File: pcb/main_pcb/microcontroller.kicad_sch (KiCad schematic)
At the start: 20 parts, among them J1 Conn_01x05, J10 Conn_01x06_Male, J2 Conn_01x05, J3 Conn_01x05, J4 Conn_01x05, J5 Conn_01x05, J6 Conn_01x05, J8 Conn_01x06_Male, U3 DRV8833

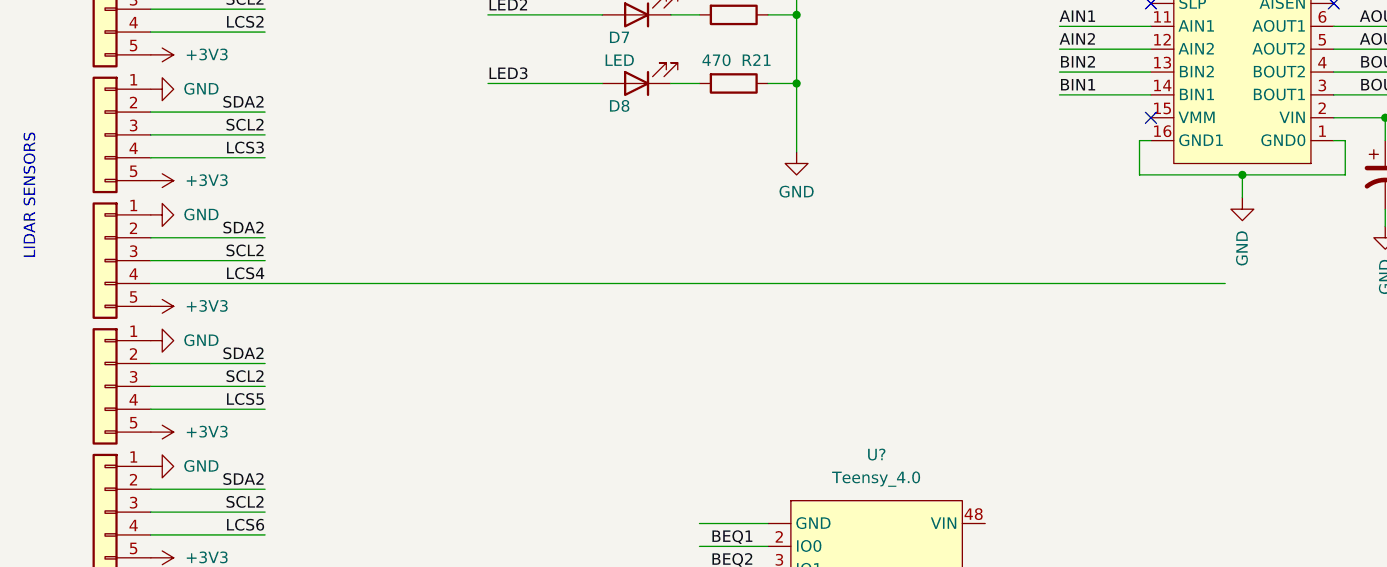
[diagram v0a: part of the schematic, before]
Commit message: Deleted old 3v3 power supply
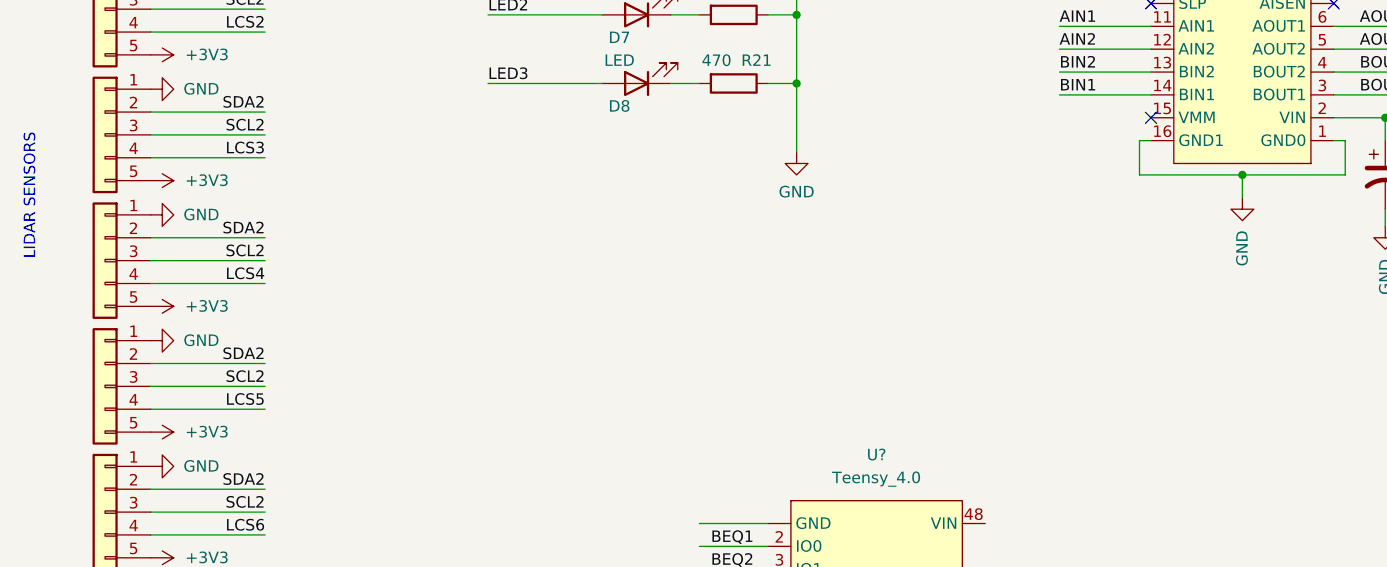
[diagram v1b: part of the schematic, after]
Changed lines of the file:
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@@
-    (stroke (width 0) (type default) (color 0 0 0 0))
-  )
-  (wire (pts (xy 35.56 81.28) (xy 154.94 81.28))
     (stroke (width 0) (type default) (color 0 0 0 0))
   )
@@
     (stroke (width 0) (type default) (color 0 0 0 0))
   )
+  (wire (pts (xy 35.56 81.28) (xy 48.26 81.28))
+    (stroke (width 0) (type default) (color 0 0 0 0))
+  )

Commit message: changes to pcb
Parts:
- gave numbers to parts that had none: 2
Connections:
- net LCS2: now reaches U2. (VBat)
- net LCS2: now also J2.4 (Pin_4)
- net LCS1: now reaches U2.20 (IO18)
- net LCS1: now also J1.4 (Pin_4)
- net LCS5: now reaches U2.22 (IO16)
- net LCS5: now also J5.4 (Pin_4)
- net LCS6: now reaches U2.23 (IO15)
- net LCS6: now also J6.4 (Pin_4)
- net LCS7: now reaches U2.24 (IO14)
- net LCS7: now also J7.4 (Pin_4)
- net LCS4: now reaches U2.8 (IO6)
- net LCS4: now also J4.4 (Pin_4)
- removed net ICSFRN: J1.4 (Pin_4), J2.4 (Pin_4), J3.4 (Pin_4), J4.4 (Pin_4), J5.4 (Pin_4), J6.4 (Pin_4), J7.4 (Pin_4), U2. (VBat), U2.16 (IO22)
- new net LCS3: J3.4 (Pin_4), U2.16 (IO22)
- no-connect marks 14 -> 9
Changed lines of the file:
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@@
   (junction (at 172.72 62.865) (diameter 0) (color 0 0 0 0)
   )
-  (junction (at 149.86 128.27) (diameter 0) (color 0 0 0 0)
-  )
-  (junction (at 149.86 130.81) (diameter 0) (color 0 0 0 0)
-  )
-  (junction (at 149.86 133.35) (diameter 0) (color 0 0 0 0)
-  )
   (junction (at 107.315 43.815) (diameter 0) (color 0 0 0 0)
   )
   (junction (at 156.845 69.215) (diameter 0) (color 0 0 0 0)
   )
-  (junction (at 149.86 135.89) (diameter 0) (color 0 0 0 0)
-  )
   (junction (at 107.315 51.435) (diameter 0) (color 0 0 0 0)
   )
-  (junction (at 149.86 125.73) (diameter 0) (color 0 0 0 0)
-  )
   (junction (at 107.315 59.055) (diameter 0) (color 0 0 0 0)
   )
-  (no_connect (at 128.27 135.89))
-  (no_connect (at 128.27 138.43))
-  (no_connect (at 104.14 125.73))
-  (no_connect (at 128.27 133.35))
   (no_connect (at 146.685 50.165))
-  (no_connect (at 128.27 128.27))
   (no_connect (at 167.005 47.625))
   (no_connect (at 146.685 62.865))
@@
     (stroke (width 0) (type default) (color 0 0 0 0))
   )
+  (wire (pts (xy 128.27 118.11) (xy 134.62 118.11))
+    (stroke (width 0) (type default) (color 0 0 0 0))
+  )
   (wire (pts (xy 85.725 51.435) (xy 73.025 51.435))
     (stroke (width 0) (type default) (color 0 0 0 0))
@@
     (stroke (width 0) (type default) (color 0 0 0 0))
   )
-  (wire (pts (xy 149.86 130.81) (xy 149.86 133.35))
-    (stroke (width 0) (type default) (color 0 0 0 0))
-  )
   (wire (pts (xy 35.56 78.74) (xy 48.26 78.74))
     (stroke (width 0) (type default) (color 0 0 0 0))
@@
     (stroke (width 0) (type default) (color 0 0 0 0))
   )
-  (wire (pts (xy 144.78 118.11) (xy 144.78 125.73))
-    (stroke (width 0) (type default) (color 0 0 0 0))
-  )
   (wire (pts (xy 96.52 133.35) (xy 104.14 133.35))
     (stroke (width 0) (type default) (color 0 0 0 0))
@@
     (stroke (width 0) (type default) (color 0 0 0 0))
   )
-  (wire (pts (xy 128.27 118.11) (xy 144.78 118.11))
+  (wire (pts (xy 128.27 138.43) (xy 135.89 138.43))
     (stroke (width 0) (type default) (color 0 0 0 0))
   )
@@
     (stroke (width 0) (type default) (color 0 0 0 0))
   )
-  (wire (pts (xy 144.78 125.73) (xy 149.86 125.73))
-    (stroke (width 0) (type default) (color 0 0 0 0))
-  )
   (wire (pts (xy 247.65 62.865) (xy 243.84 62.865))
     (stroke (width 0) (type default) (color 0 0 0 0))
@@
     (stroke (width 0) (type default) (color 0 0 0 0))
   )
-  (wire (pts (xy 149.86 125.73) (xy 154.94 125.73))
-    (stroke (width 0) (type default) (color 0 0 0 0))
-  )
   (wire (pts (xy 35.56 67.31) (xy 48.26 67.31))
     (stroke (width 0) (type default) (color 0 0 0 0))
@@
     (stroke (width 0) (type default) (color 0 0 0 0))
   )
+  (wire (pts (xy 128.27 135.89) (xy 135.89 135.89))
+    (stroke (width 0) (type default) (color 0 0 0 0))
+  )
   (wire (pts (xy 107.315 43.815) (xy 107.315 51.435))
     (stroke (width 0) (type default) (color 0 0 0 0))
@@
     (stroke (width 0) (type default) (color 0 0 0 0))
   )
-  (wire (pts (xy 149.86 125.73) (xy 149.86 128.27))
-    (stroke (width 0) (type default) (color 0 0 0 0))
-  )
   (wire (pts (xy 35.56 76.2) (xy 48.26 76.2))
     (stroke (width 0) (type default) (color 0 0 0 0))
@@
     (stroke (width 0) (type default) (color 0 0 0 0))
   )
+  (wire (pts (xy 128.27 128.27) (xy 135.89 128.27))
+    (stroke (width 0) (type default) (color 0 0 0 0))
+  )
   (wire (pts (xy 107.315 59.055) (xy 107.315 66.675))
     (stroke (width 0) (type default) (color 0 0 0 0))
   )
-  (wire (pts (xy 149.86 135.89) (xy 149.86 138.43))
-    (stroke (width 0) (type default) (color 0 0 0 0))
-  )
-  (wire (pts (xy 149.86 128.27) (xy 149.86 130.81))
-    (stroke (width 0) (type default) (color 0 0 0 0))
-  )
   (wire (pts (xy 146.685 55.245) (xy 136.525 55.245))
     (stroke (width 0) (type default) (color 0 0 0 0))
@@
     (stroke (width 0) (type default) (color 0 0 0 0))
   )
-  (wire (pts (xy 149.86 138.43) (xy 154.94 138.43))
-    (stroke (width 0) (type default) (color 0 0 0 0))
-  )
   (wire (pts (xy 35.56 121.92) (xy 48.26 121.92))
     (stroke (width 0) (type default) (color 0 0 0 0))
@@
     (stroke (width 0) (type default) (color 0 0 0 0))
   )
-  (wire (pts (xy 149.86 128.27) (xy 154.94 128.27))
-    (stroke (width 0) (type default) (color 0 0 0 0))
-  )
   (wire (pts (xy 202.565 45.085) (xy 202.565 55.245))
     (stroke (width 0) (type default) (color 0 0 0 0))
@@
     (stroke (width 0) (type default) (color 0 0 0 0))
   )
+  (wire (pts (xy 96.52 125.73) (xy 104.14 125.73))
+    (stroke (width 0) (type default) (color 0 0 0 0))
+  )
   (wire (pts (xy 104.14 59.055) (xy 107.315 59.055))
     (stroke (width 0) (type default) (color 0 0 0 0))
@@
     (stroke (width 0) (type default) (color 0 0 0 0))
   )
-  (wire (pts (xy 149.86 133.35) (xy 154.94 133.35))
-    (stroke (width 0) (type default) (color 0 0 0 0))
-  )
-  (wire (pts (xy 149.86 135.89) (xy 154.94 135.89))
-    (stroke (width 0) (type default) (color 0 0 0 0))
-  )
-  (wire (pts (xy 149.86 130.81) (xy 154.94 130.81))
-    (stroke (width 0) (type default) (color 0 0 0 0))
-  )
   (wire (pts (xy 35.56 109.22) (xy 48.26 109.22))
     (stroke (width 0) (type default) (color 0 0 0 0))
@@
     (stroke (width 0) (type default) (color 0 0 0 0))
   )
-  (wire (pts (xy 149.86 133.35) (xy 149.86 135.89))
-    (stroke (width 0) (type default) (color 0 0 0 0))
-  )
-  (wire (pts (xy 149.86 125.73) (xy 149.86 123.19))
-    (stroke (width 0) (type default) (color 0 0 0 0))
-  )
   (wire (pts (xy 93.345 43.815) (xy 96.52 43.815))
     (stroke (width 0) (type default) (color 0 0 0 0))
@@
     (stroke (width 0) (type default) (color 0 0 0 0))
   )
+  (wire (pts (xy 128.27 133.35) (xy 135.89 133.35))
+    (stroke (width 0) (type default) (color 0 0 0 0))
+  )
   (wire (pts (xy 35.56 64.77) (xy 48.26 64.77))
     (stroke (width 0) (type default) (color 0 0 0 0))
@@
   )
   (wire (pts (xy 191.135 60.325) (xy 203.835 60.325))
-    (stroke (width 0) (type default) (color 0 0 0 0))
-  )
-  (wire (pts (xy 149.86 123.19) (xy 154.94 123.19))
     (stroke (width 0) (type default) (color 0 0 0 0))
   )
@@
     (effects (font (size 1.27 1.27)) (justify right bottom))
   )
-  (label "LCS4" (at 149.86 130.81 0)
+  (label "LCS4" (at 96.52 125.73 0)
     (effects (font (size 1.27 1.27)) (justify left bottom))
   )
@@
     (effects (font (size 1.27 1.27)) (justify right bottom))
   )
-  (label "LCS7" (at 149.86 138.43 0)
+  (label "LCS7" (at 129.54 138.43 0)
     (effects (font (size 1.27 1.27)) (justify left bottom))
   )
@@
     (effects (font (size 1.27 1.27)) (justify left bottom))
   )
-  (label "ICSFRN" (at 128.27 115.57 0)
-    (effects (font (size 1.27 1.27)) (justify left bottom))
-  )
-  (label "LCS2" (at 149.86 125.73 0)
+  (label "LCS2" (at 129.54 115.57 0)
     (effects (font (size 1.27 1.27)) (justify left bottom))
   )
@@
     (effects (font (size 1.27 1.27)) (justify left bottom))
   )
-  (label "LCS3" (at 149.86 128.27 0)
-    (effects (font (size 1.27 1.27)) (justify left bottom))
-  )
   (label "LED2" (at 129.54 123.19 0)
     (effects (font (size 1.27 1.27)) (justify left bottom))
   )
-  (label "LCS1" (at 149.86 123.19 0)
+  (label "LCS1" (at 129.54 128.27 0)
     (effects (font (size 1.27 1.27)) (justify left bottom))
   )
@@
     (effects (font (size 1.27 1.27)) (justify left bottom))
   )
-  (label "ICSFRN" (at 128.27 118.11 0)
-    (effects (font (size 1.27 1.27)) (justify left bottom))
-  )
   (label "LED1" (at 97.79 123.19 0)
     (effects (font (size 1.27 1.27)) (justify left bottom))
   )
+  (label "LCS3" (at 129.54 118.11 0)
+    (effects (font (size 1.27 1.27)) (justify left bottom))
+  )
   (label "SCL2" (at 129.54 130.81 0)
     (effects (font (size 1.27 1.27)) (justify left bottom))
@@
     (effects (font (size 1.27 1.27)) (justify right bottom))
   )
+  (label "LCS6" (at 129.54 135.89 0)
+    (effects (font (size 1.27 1.27)) (justify left bottom))
+  )
   (label "SCL2" (at 48.26 92.71 180)
     (effects (font (size 1.27 1.27)) (justify right bottom))
@@
     (effects (font (size 1.27 1.27)) (justify left bottom))
   )
-  (label "LCS6" (at 149.86 135.89 0)
-    (effects (font (size 1.27 1.27)) (justify left bottom))
-  )
   (label "AIN1" (at 97.79 115.57 0)
     (effects (font (size 1.27 1.27)) (justify left bottom))
@@
     (effects (font (size 1.27 1.27)) (justify left bottom))
   )
-  (label "LCS5" (at 149.86 133.35 0)
+  (label "LCS5" (at 129.54 133.35 0)
     (effects (font (size 1.27 1.27)) (justify left bottom))
   )
@@
   (symbol (lib_id "power:GND") (at 35.56 116.84 90) (unit 1)
     (in_bom yes) (on_board yes)
-    (property "Reference" "#PWR?" (id 0) (at 41.91 116.84 0)
+    (property "Reference" "#PWR0102" (id 0) (at 41.91 116.84 0)
       (effects (font (size 1.27 1.27)) hide)
     )
@@
   (symbol (lib_name "Teensy_4.1_1") (lib_id "sym_library:Teensy_4.1") (at 93.98 130.81 0) (unit 1)
     (in_bom yes) (on_board yes) (fields_autoplaced)
-    (property "Reference" "U?" (id 0) (at 116.205 100.33 0))
+    (property "Reference" "U2" (id 0) (at 116.205 100.33 0))
     (property "Value" "Teensy_4.0" (id 1) (at 116.205 102.87 0))
     (property "Footprint" "" (id 2) (at 93.98 130.81 0)
@@
   (symbol (lib_id "power:+3V3") (at 35.56 127 270) (unit 1)
     (in_bom yes) (on_board yes) (fields_autoplaced)
-    (property "Reference" "#PWR?" (id 0) (at 31.75 127 0)
+    (property "Reference" "#PWR0101" (id 0) (at 31.75 127 0)
       (effects (font (size 1.27 1.27)) hide)
     )
@@
   (symbol (lib_id "Connector_Generic:Conn_01x05") (at 30.48 121.92 0) (mirror y) (unit 1)
     (in_bom yes) (on_board yes) (fields_autoplaced)
-    (property "Reference" "J?" (id 0) (at 30.48 133.35 0)
-      (effects (font (size 1.27 1.27)) hide)
-    )
+    (property "Reference" "J7" (id 0) (at 30.48 133.35 0)
+      (effects (font (size 1.27 1.27)) hide)
+    )

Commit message: Error corrections
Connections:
- net +BATT: now also U2.48 (VIN)
- net GND: now also U2. (VBat)
- no-connect marks 9 -> 14
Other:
- moved on the sheet: U2
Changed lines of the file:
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@@
   (junction (at 107.315 59.055) (diameter 0) (color 0 0 0 0)
   )
+  (no_connect (at 111.76 151.13))
+  (no_connect (at 119.38 151.13))
+  (no_connect (at 114.3 151.13))
+  (no_connect (at 121.92 151.13))
   (no_connect (at 146.685 50.165))
   (no_connect (at 167.005 47.625))
@@
   (no_connect (at 167.005 50.165))
   (no_connect (at 146.685 47.625))
-  (no_connect (at 104.14 128.27))
-  (no_connect (at 128.27 120.65))
-  (no_connect (at 128.27 140.97))
-  (no_connect (at 104.14 135.89))
+  (no_connect (at 116.84 151.13))
+  (no_connect (at 105.41 128.27))
+  (no_connect (at 129.54 120.65))
+  (no_connect (at 129.54 140.97))
+  (no_connect (at 105.41 135.89))
   (wire (pts (xy 35.56 39.37) (xy 48.26 39.37))
     (stroke (width 0) (type default) (color 0 0 0 0))
   )
-  (wire (pts (xy 128.27 118.11) (xy 134.62 118.11))
+  (wire (pts (xy 129.54 118.11) (xy 134.62 118.11))
     (stroke (width 0) (type default) (color 0 0 0 0))
   )
@@
     (stroke (width 0) (type default) (color 0 0 0 0))
   )
-  (wire (pts (xy 96.52 130.81) (xy 104.14 130.81))
+  (wire (pts (xy 96.52 130.81) (xy 105.41 130.81))
     (stroke (width 0) (type default) (color 0 0 0 0))
   )
@@
     (stroke (width 0) (type default) (color 0 0 0 0))
   )
-  (wire (pts (xy 96.52 115.57) (xy 104.14 115.57))
+  (wire (pts (xy 96.52 115.57) (xy 105.41 115.57))
     (stroke (width 0) (type default) (color 0 0 0 0))
   )
@@
     (stroke (width 0) (type default) (color 0 0 0 0))
   )
-  (wire (pts (xy 96.52 133.35) (xy 104.14 133.35))
+  (wire (pts (xy 96.52 133.35) (xy 105.41 133.35))
     (stroke (width 0) (type default) (color 0 0 0 0))
   )
@@
     (stroke (width 0) (type default) (color 0 0 0 0))
   )
-  (wire (pts (xy 128.27 138.43) (xy 135.89 138.43))
-    (stroke (width 0) (type default) (color 0 0 0 0))
-  )
-  (wire (pts (xy 128.27 123.19) (xy 135.89 123.19))
+  (wire (pts (xy 129.54 138.43) (xy 135.89 138.43))
+    (stroke (width 0) (type default) (color 0 0 0 0))
+  )
+  (wire (pts (xy 129.54 123.19) (xy 135.89 123.19))
     (stroke (width 0) (type default) (color 0 0 0 0))
   )
@@
     (stroke (width 0) (type default) (color 0 0 0 0))
   )
-  (wire (pts (xy 128.27 115.57) (xy 134.62 115.57))
+  (wire (pts (xy 129.54 115.57) (xy 134.62 115.57))
     (stroke (width 0) (type default) (color 0 0 0 0))
   )
@@
     (stroke (width 0) (type default) (color 0 0 0 0))
   )
-  (wire (pts (xy 96.52 118.11) (xy 104.14 118.11))
-    (stroke (width 0) (type default) (color 0 0 0 0))
-  )
-  (wire (pts (xy 96.52 113.03) (xy 104.14 113.03))
+  (wire (pts (xy 96.52 118.11) (xy 105.41 118.11))
+    (stroke (width 0) (type default) (color 0 0 0 0))
+  )
+  (wire (pts (xy 96.52 113.03) (xy 105.41 113.03))
     (stroke (width 0) (type default) (color 0 0 0 0))
   )
@@
     (stroke (width 0) (type default) (color 0 0 0 0))
   )
-  (wire (pts (xy 96.52 140.97) (xy 104.14 140.97))
-    (stroke (width 0) (type default) (color 0 0 0 0))
-  )
-  (wire (pts (xy 128.27 135.89) (xy 135.89 135.89))
+  (wire (pts (xy 96.52 140.97) (xy 105.41 140.97))
+    (stroke (width 0) (type default) (color 0 0 0 0))
+  )
+  (wire (pts (xy 129.54 135.89) (xy 135.89 135.89))
     (stroke (width 0) (type default) (color 0 0 0 0))
   )
@@
     (stroke (width 0) (type default) (color 0 0 0 0))
   )
-  (wire (pts (xy 96.52 107.95) (xy 104.14 107.95))
+  (wire (pts (xy 96.52 107.95) (xy 105.41 107.95))
     (stroke (width 0) (type default) (color 0 0 0 0))
   )
@@
     (stroke (width 0) (type default) (color 0 0 0 0))
   )
-  (wire (pts (xy 128.27 128.27) (xy 135.89 128.27))
+  (wire (pts (xy 129.54 128.27) (xy 135.89 128.27))
     (stroke (width 0) (type default) (color 0 0 0 0))
   )
@@
     (stroke (width 0) (type default) (color 0 0 0 0))
   )
-  (wire (pts (xy 128.27 125.73) (xy 135.89 125.73))
+  (wire (pts (xy 129.54 125.73) (xy 135.89 125.73))
     (stroke (width 0) (type default) (color 0 0 0 0))
   )
@@
     (stroke (width 0) (type default) (color 0 0 0 0))
   )
-  (wire (pts (xy 96.52 123.19) (xy 104.14 123.19))
+  (wire (pts (xy 96.52 123.19) (xy 105.41 123.19))
     (stroke (width 0) (type default) (color 0 0 0 0))
   )
@@
     (stroke (width 0) (type default) (color 0 0 0 0))
   )
-  (wire (pts (xy 96.52 125.73) (xy 104.14 125.73))
+  (wire (pts (xy 96.52 125.73) (xy 105.41 125.73))
     (stroke (width 0) (type default) (color 0 0 0 0))
   )
@@
     (stroke (width 0) (type default) (color 0 0 0 0))
   )
-  (wire (pts (xy 96.52 110.49) (xy 104.14 110.49))
+  (wire (pts (xy 96.52 110.49) (xy 105.41 110.49))
     (stroke (width 0) (type default) (color 0 0 0 0))
   )
@@
     (stroke (width 0) (type default) (color 0 0 0 0))
   )
-  (wire (pts (xy 96.52 138.43) (xy 104.14 138.43))
+  (wire (pts (xy 129.54 107.95) (xy 128.27 107.95))
+    (stroke (width 0) (type default) (color 0 0 0 0))
+  )
+  (wire (pts (xy 96.52 138.43) (xy 105.41 138.43))
     (stroke (width 0) (type default) (color 0 0 0 0))
   )
@@
     (stroke (width 0) (type default) (color 0 0 0 0))
   )
-  (wire (pts (xy 128.27 130.81) (xy 135.89 130.81))
-    (stroke (width 0) (type default) (color 0 0 0 0))
-  )
-  (wire (pts (xy 128.27 133.35) (xy 135.89 133.35))
+  (wire (pts (xy 129.54 130.81) (xy 135.89 130.81))
+    (stroke (width 0) (type default) (color 0 0 0 0))
+  )
+  (wire (pts (xy 129.54 133.35) (xy 135.89 133.35))
     (stroke (width 0) (type default) (color 0 0 0 0))
   )
@@
     (stroke (width 0) (type default) (color 0 0 0 0))
   )
-  (wire (pts (xy 96.52 120.65) (xy 104.14 120.65))
+  (wire (pts (xy 96.52 120.65) (xy 105.41 120.65))
     (stroke (width 0) (type default) (color 0 0 0 0))
   )
@@
     (pin "9")
   )
-  (symbol (lib_name "Teensy_4.1_1") (lib_id "sym_library:Teensy_4.1") (at 93.98 130.81 0) (unit 1)
-    (in_bom yes) (on_board yes) (fields_autoplaced)
-    (property "Reference" "U2" (id 0) (at 116.205 100.33 0))
-    (property "Value" "Teensy_4.0" (id 1) (at 116.205 102.87 0))
-    (property "Footprint" "" (id 2) (at 93.98 130.81 0)
-      (effects (font (size 1.27 1.27)) hide)
-    )
-    (property "Datasheet" "" (id 3) (at 93.98 130.81 0)
+  (symbol (lib_name "Teensy_4.1_1") (lib_id "sym_library:Teensy_4.1") (at 95.25 130.81 0) (unit 1)
+    (in_bom yes) (on_board yes) (fields_autoplaced)
+    (property "Reference" "U2" (id 0) (at 117.475 100.33 0))
+    (property "Value" "Teensy_4.0" (id 1) (at 117.475 102.87 0))
+    (property "Footprint" "" (id 2) (at 95.25 130.81 0)
+      (effects (font (size 1.27 1.27)) hide)
+    )
+    (property "Datasheet" "" (id 3) (at 95.25 130.81 0)
       (effects (font (size 1.27 1.27)) hide)
     )
@@
     (pin "1")
   )
+  (symbol (lib_name "GND_1") (lib_id "power:GND") (at 96.52 107.95 270) (unit 1)
+    (in_bom yes) (on_board yes) (fields_autoplaced)
+    (property "Reference" "#PWR0112" (id 0) (at 90.17 107.95 0)
+      (effects (font (size 1.27 1.27)) hide)
+    )
+    (property "Value" "GND" (id 1) (at 92.71 107.9499 90)
+      (effects (font (size 1.27 1.27)) (justify right))
+    )
+    (property "Footprint" "" (id 2) (at 96.52 107.95 0)
+      (effects (font (size 1.27 1.27)) hide)
+    )
+    (property "Datasheet" "" (id 3) (at 96.52 107.95 0)
+      (effects (font (size 1.27 1.27)) hide)
+    )
+    (pin "1")
+  )
   (symbol (lib_id "Device:R") (at 100.33 36.195 270) (unit 1)
     (in_bom yes) (on_board yes)
@@
       (effects (font (size 1.27 1.27)) hide)
     )
+    (pin "1")
+  )
+  (symbol (lib_id "power:+BATT") (at 128.27 107.95 270) (unit 1)
+    (in_bom yes) (on_board yes) (fields_autoplaced)
+    (property "Reference" "#PWR0113" (id 0) (at 124.46 107.95 0)
+      (effects (font (size 1.27 1.27)) hide)
+    )
+    (property "Value" "+BATT" (id 1) (at 131.445 107.9499 90)
+      (effects (font (size 1.27 1.27)) (justify left))
+    )
+    (property "Footprint" "" (id 2) (at 128.27 107.95 0)
+      (effects (font (size 1.27 1.27)) hide)
+    )
+    (property "Datasheet" "" (id 3) (at 128.27 107.95 0)
+      (effects (font (size 1.27 1.27)) hide)
+    )
